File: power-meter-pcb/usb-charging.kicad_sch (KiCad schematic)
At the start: 30 parts, among them J3 USB4120-03-C_REVA, J4 Battery, Q1 AS2302, Q2 AS2302, U3 MCP73831-2-OT, U4 TPD3E001DRLR, U5 S-8261AAJMD-G2JT2U, U6 TPS63031DSK

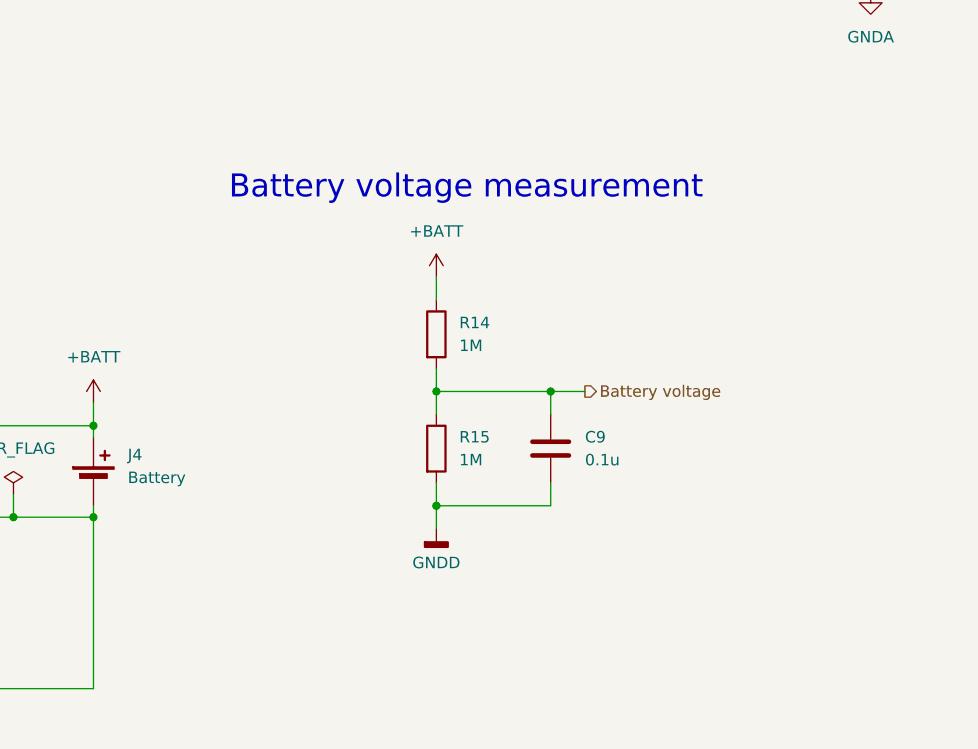
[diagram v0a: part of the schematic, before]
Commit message: Cleaning up PCB back and title box
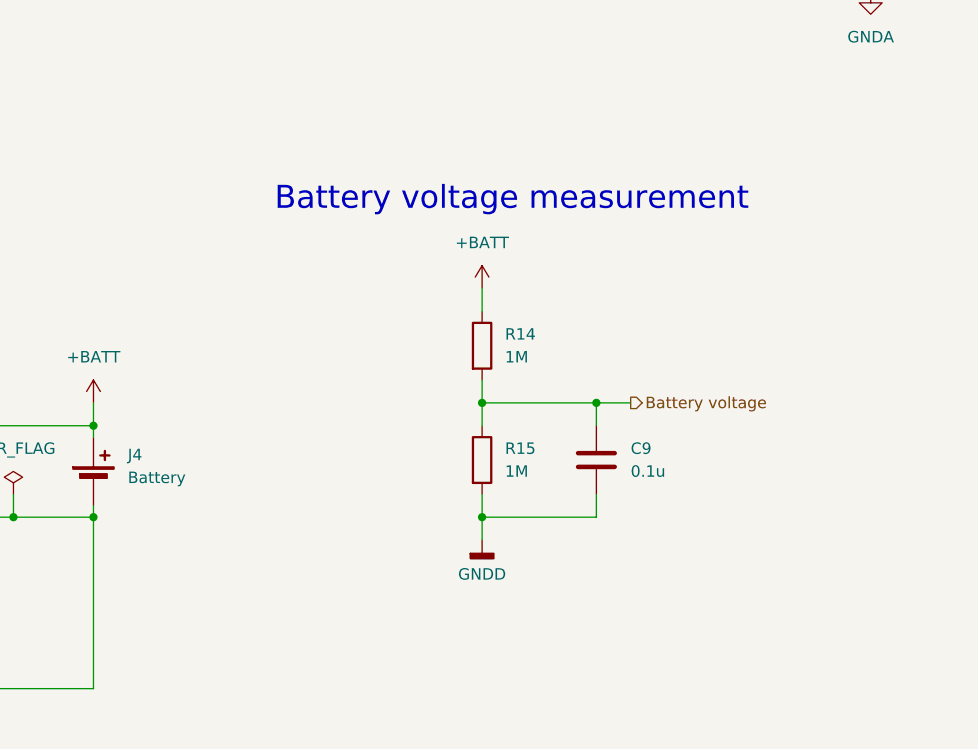
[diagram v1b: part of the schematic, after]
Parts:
- C10, C11, C5, C7, C8, FB1, L1, R16, U6: PlaceOnSecondary (none) -> Yes
- C3, C4, C6, C9, D4, D5, J3, J4, Q1, Q2, R10, R11, R12, R13, R14, R15, R8, R9, U3, U4, U5: PlaceOnSecondary (none) -> No
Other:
- moved on the sheet: C9, R14, R15

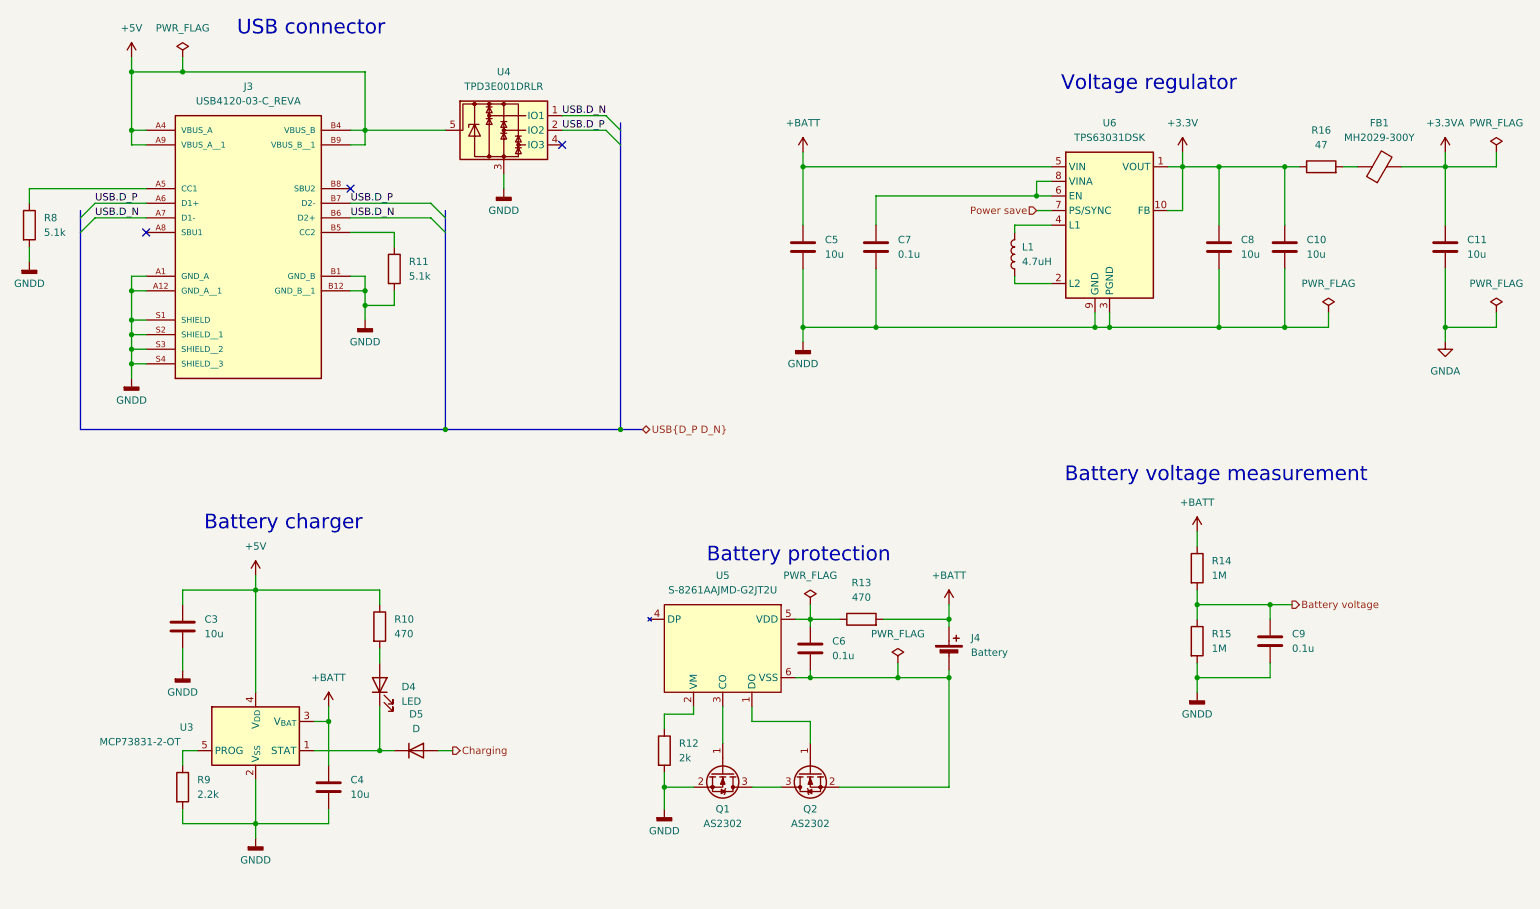
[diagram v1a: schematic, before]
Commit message: Smaller PCB design started
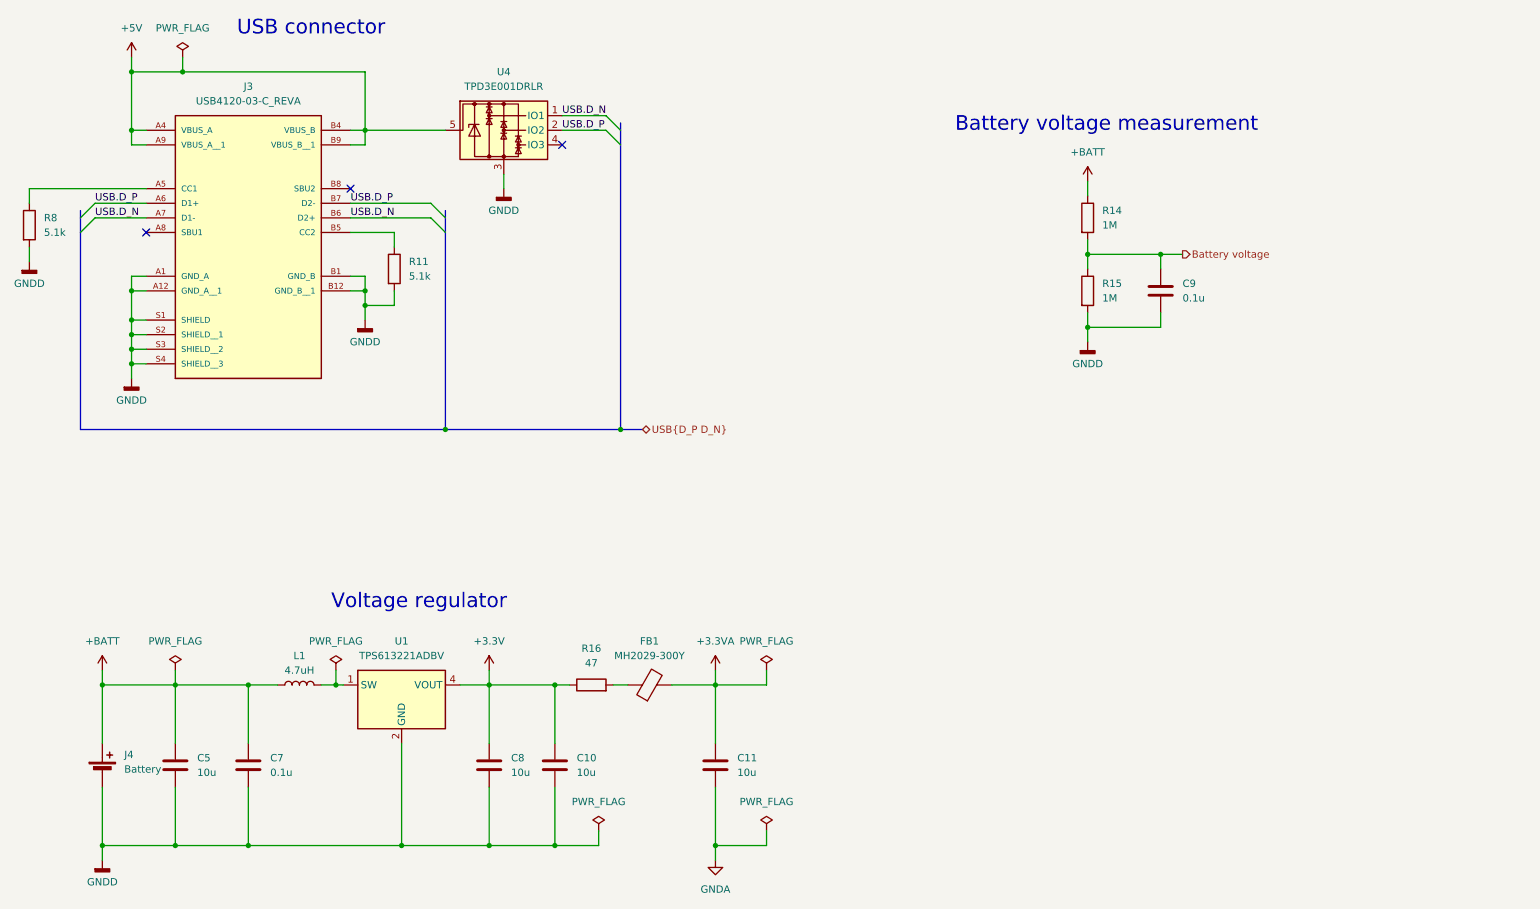
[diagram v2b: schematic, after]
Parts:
- removed C3, C4: 10u, Capacitor_SMD:C_0603_1608Metric_Pad1.08x0.95mm_HandSolder, symbol Device:C
- removed C6: 0.1u, Capacitor_SMD:C_0603_1608Metric_Pad1.08x0.95mm_HandSolder, symbol Device:C
- removed D4: LED, LED_SMD:LED_0603_1608Metric_Pad1.05x0.95mm_HandSolder, symbol Device:LED
- removed D5: D, Diode_SMD:D_0603_1608Metric_Pad1.05x0.95mm_HandSolder, symbol Device:D
- removed Q1, Q2: AS2302, Package_TO_SOT_SMD:TSOT-23, symbol Device:Q_NMOS_GSD
- removed R10, R13: 470, Resistor_SMD:R_0603_1608Metric_Pad0.98x0.95mm_HandSolder, symbol Device:R
- removed R12: 2k, Resistor_SMD:R_0603_1608Metric_Pad0.98x0.95mm_HandSolder, symbol Device:R
- removed R9: 2.2k, Resistor_SMD:R_0603_1608Metric_Pad0.98x0.95mm_HandSolder, symbol Device:R
- removed U3: MCP73831-2-OT, Package_TO_SOT_SMD:SOT-23-5, symbol Battery_Management:MCP73831-2-OT
- removed U5: S-8261AAJMD-G2JT2U, Package_TO_SOT_SMD:SOT-23-6, symbol Custom:S-8261_Battery_protection_IC
- removed U6: TPS63031DSK, Package_SON:WSON-10-1EP_2.5x2.5mm_P0.5mm_EP1.2x2mm, symbol Regulator_Switching:TPS63031DSK
- added U1: TPS613221ADBV, Package_TO_SOT_SMD:SOT-23-5, symbol Regulator_Switching:TPS613221ADBV
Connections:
- net +3.3V: now also U1.4 (VOUT)
- net +BATT: now also C7.1, L1.1
- net GNDD: now also J4.2 (-), U1.2 (GND)
- net at L1.2: now also U1.1 (SW)
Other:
- note removed: "Battery charger"
- note removed: "Battery protection"
- moved on the sheet: C10, C11, C5, C7, C8, C9, FB1, J4, L1, R14, R15, R16

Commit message: Board mostly routed, schematic page layout cleaned up
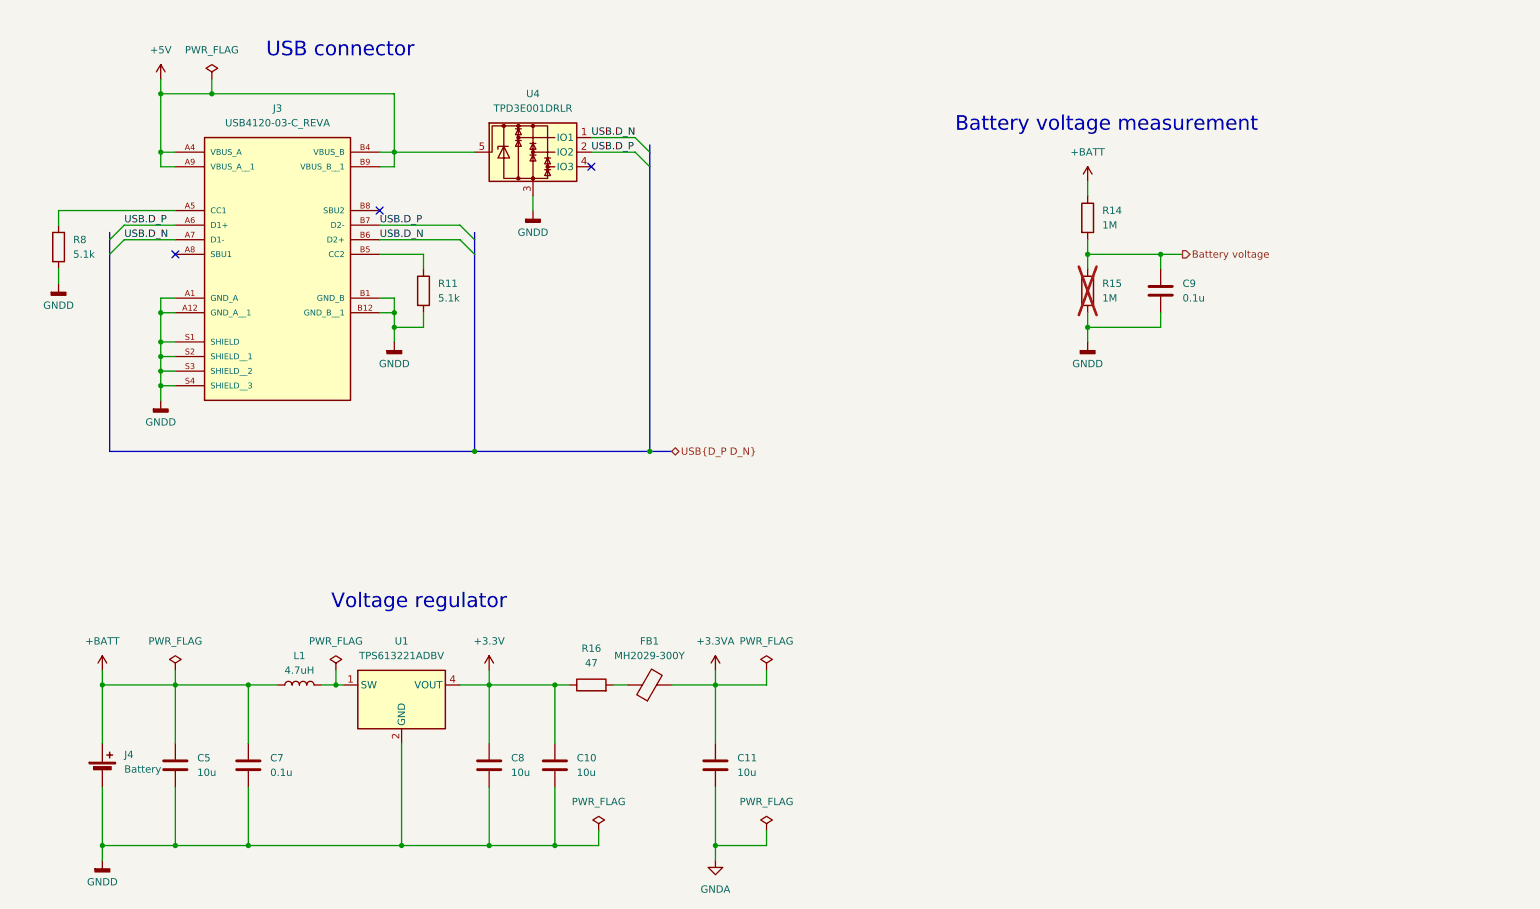
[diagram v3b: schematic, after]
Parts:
- R15: now not fitted
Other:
- moved on the sheet: J3, R11, R8, U4

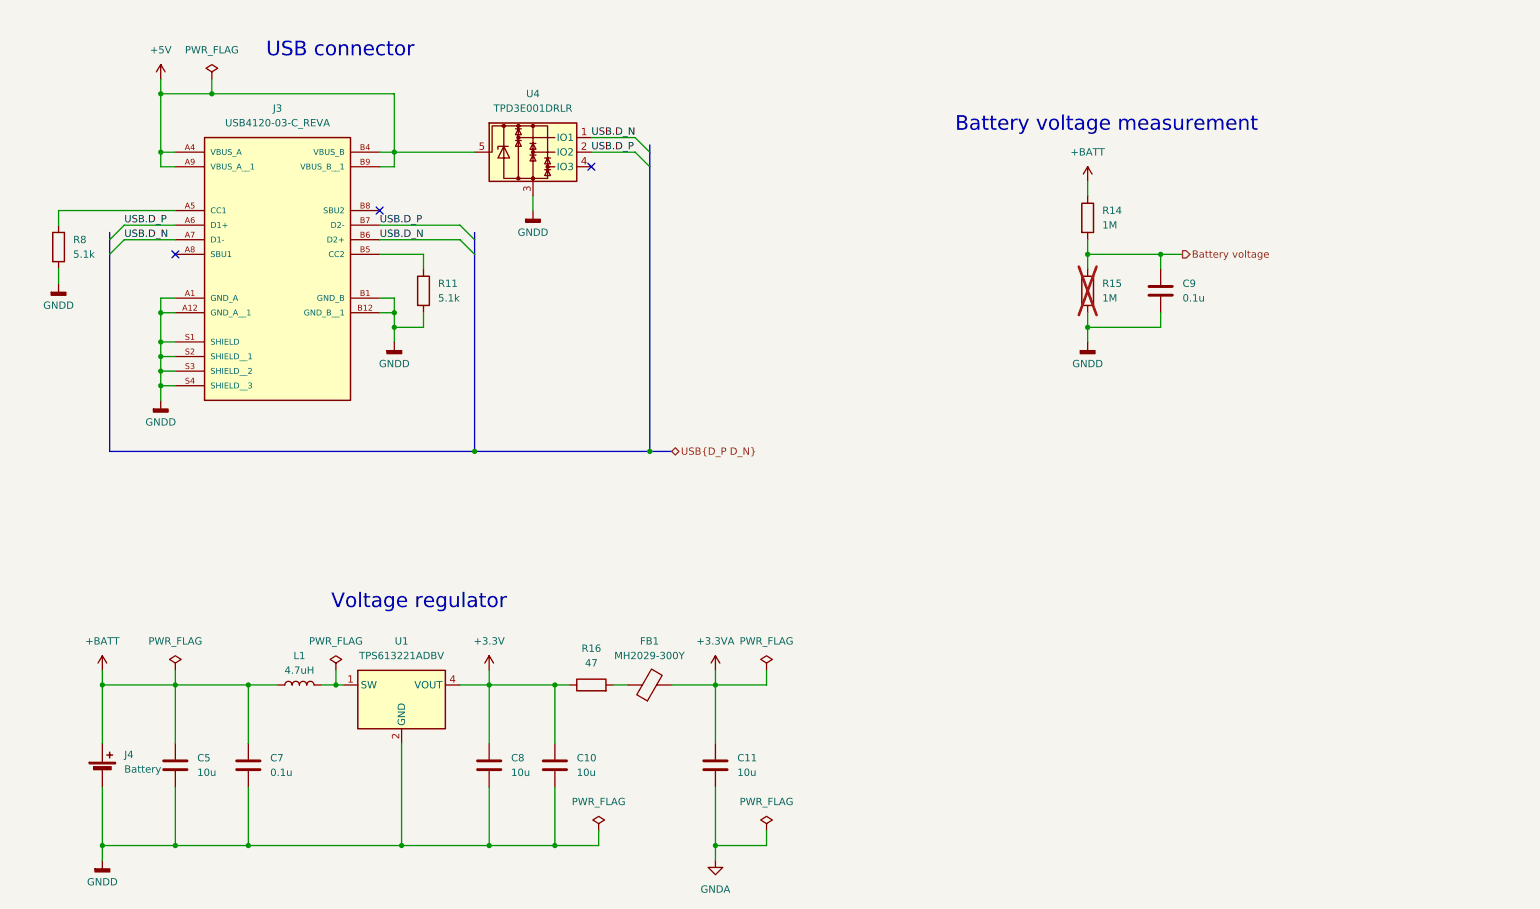
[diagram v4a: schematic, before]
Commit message: Re-centred schematics, added header for spare GPIO pins, touched up logos
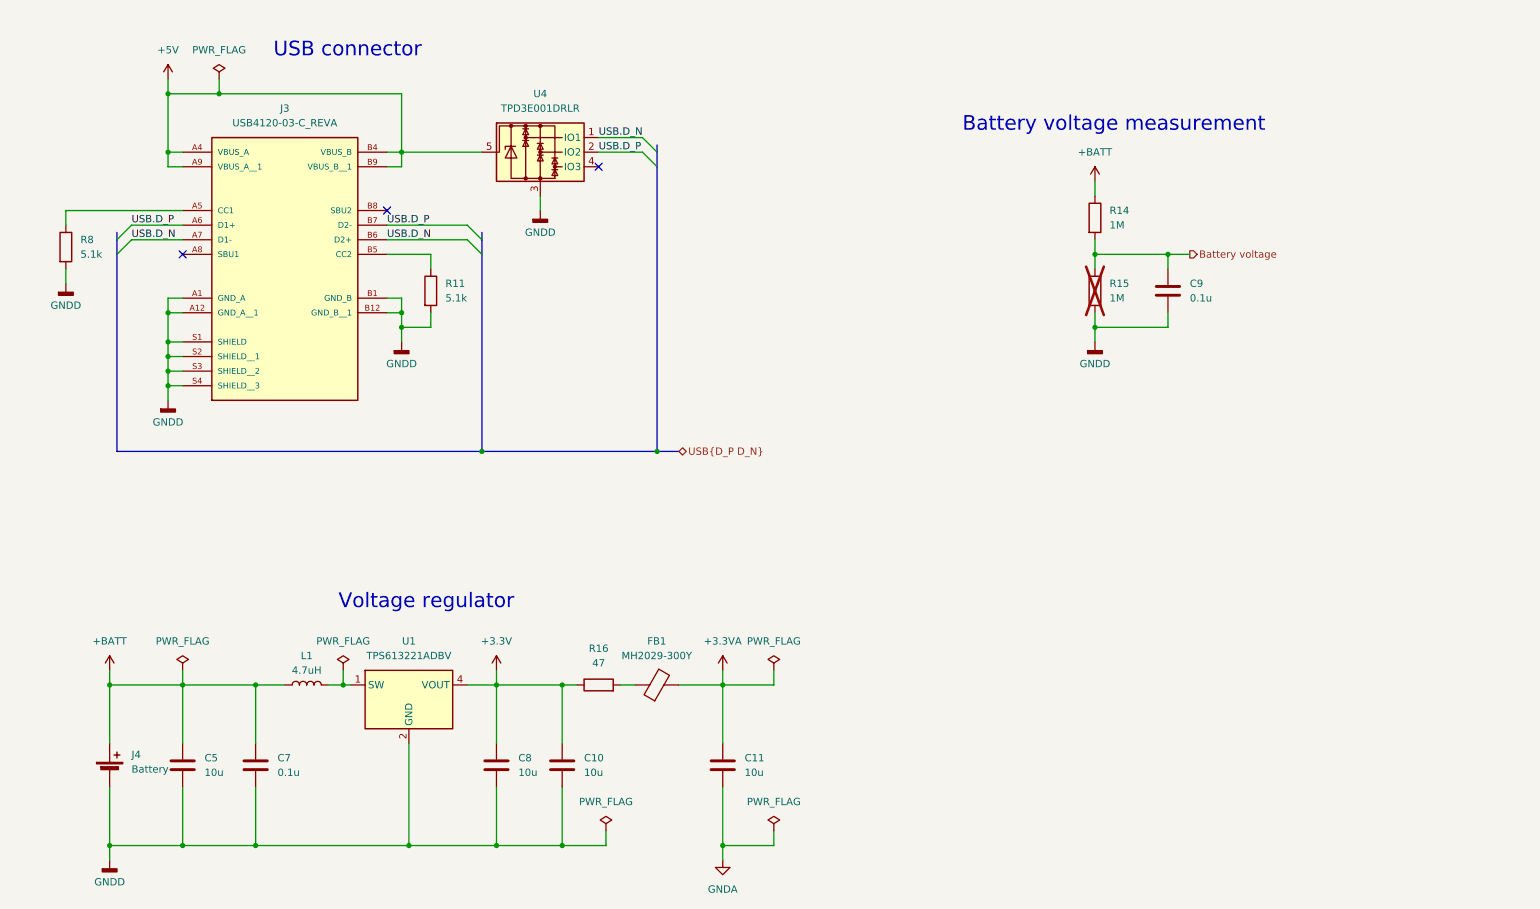
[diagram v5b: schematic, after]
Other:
- moved on the sheet: C10, C11, C5, C7, C8, C9, FB1, J3, J4, L1, R11, R14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

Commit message: Added LED driven by temp sensor, updated numbering
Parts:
- U3: renamed from U1; PlaceOnSecondary (none) -> Yes
- renumbered C5 to C3, C7 to C4, C8 to C5, C10 to C6, C11 to C7, C9 to C8, J3 to J5, R16 to R10, R14 to R11, R15 to R12, R11 to R9
